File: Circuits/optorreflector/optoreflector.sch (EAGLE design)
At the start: 9 parts, among them IC1 LM358D

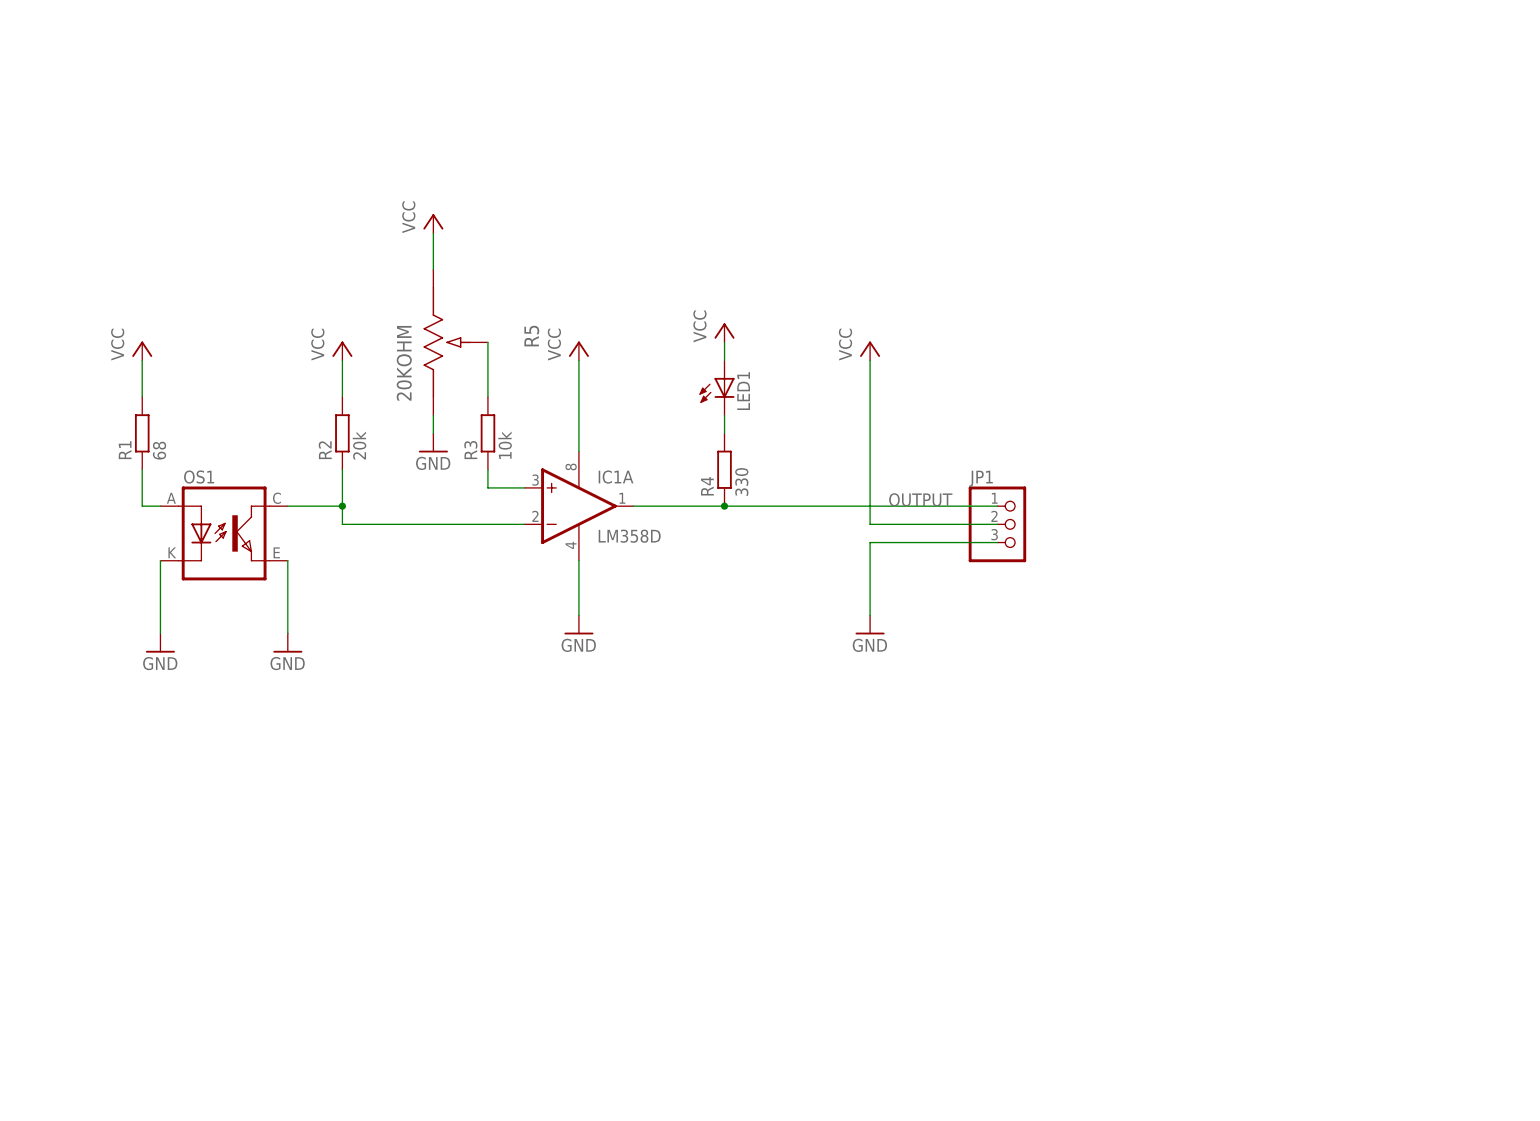
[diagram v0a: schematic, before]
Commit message: ❌ Deleted unused files
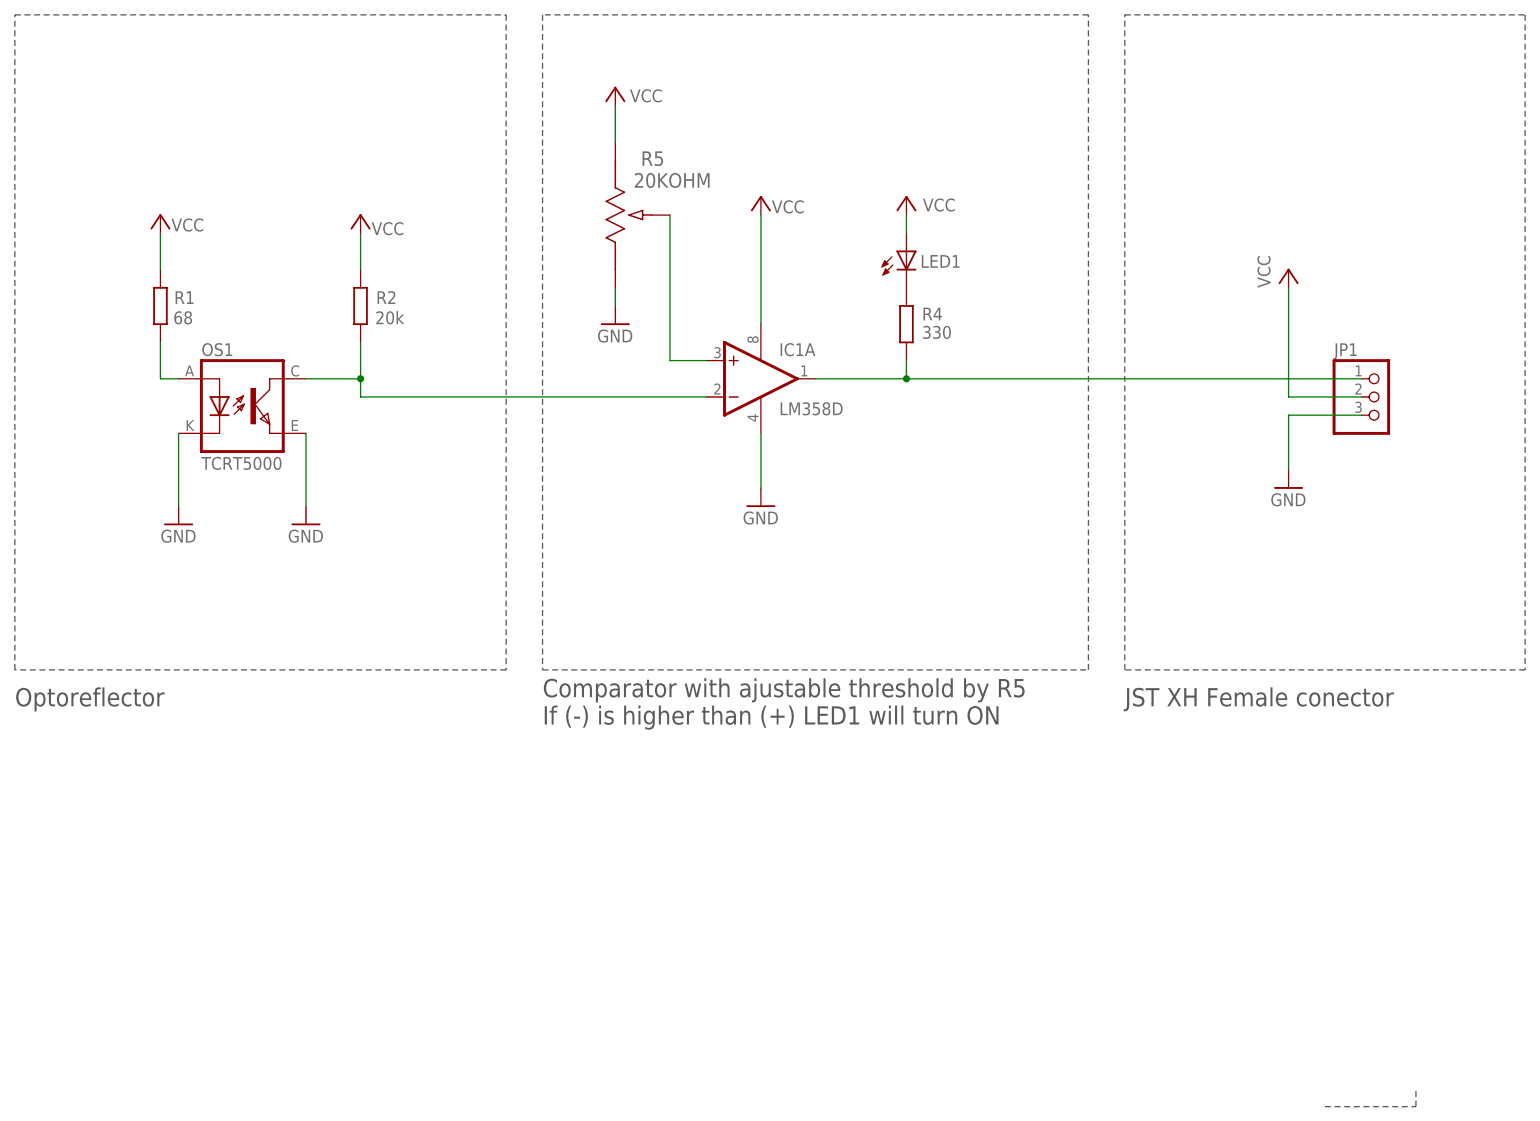
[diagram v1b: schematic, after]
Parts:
- removed R3: 10k, rcl:R-EU_R0805
- OS1: value (none) -> TCRT5000
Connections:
- net OUTPUT renamed N$5
- removed net N$5 (its old number): IC1A.+IN, R3.1
- net N$4: now also IC1A.+IN; no longer R3.2
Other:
- note added: "Comparator with ajustable threshold by R5 If (-) is higher than (+) LED1 will turn ON"
- note added: "JST XH Female conector"
- note added: "Optoreflector"
- moved on the sheet: IC1A, JP1, LED1, OS1, R1, R2, R4, R5
